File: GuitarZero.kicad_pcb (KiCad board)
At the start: 2 copper layers, 142 parts, among them J1 USB_A, J2 USB_B_Micro, J3 AudioJack3_SwitchT, J4 FPGA_Debug, J6 Micro_SD_Card_Det_Hirose_DM3AT, SW1 SW_Push, SW2 SW_Push, SW3 SW_Push, SW4 SW_Push, SW5 SW_Push, SW6 SW_Push, U1 TPS54325, U10 FPGA_GPIO_Extra, U11 5x7 LED_matrix, U12 MCU_GPIO_Extra, U13 5x7 LED_matrix, U14 Power_Jumpers, U2 TSP54294, U3 XC7A100T-FTG256, U4 EFM32GG332, U5 S25FL127S, U6 Oscillator, U7 FPGA_JTAG_Debug, U8 PCM1754, U9 TPD_Current_Switch, Y1 Crystal_GND23

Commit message: First pass at placing components physically
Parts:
- J4: value FPGA_Debug -> MCU_Debug
- moved U10 140.1 mm to (239.0, 67.2)
- moved R14 131.9 mm to (232.0, 97.0), turned to 180 degrees
- moved R15 131.9 mm to (232.0, 100.3), turned to 180 degrees
- moved R16 131.9 mm to (232.0, 103.6), turned to 180 degrees
- moved R17 131.8 mm to (232.0, 107.0)
- moved R13 131.8 mm to (232.0, 94.0), turned to 180 degrees
- moved U7 131.3 mm to (239.2, 93.2)
- moved U6 127.5 mm to (218.0, 80.0)
- moved R34 123.6 mm to (201.0, 72.4)
- moved R35 123.6 mm to (201.0, 75.7)
- moved U12 121.6 mm to (153.9, 180.0), turned to 90 degrees
- moved C53 120.7 mm to (222.0, 74.0)
- moved D1 116.9 mm to (209.9, 71.0)
- moved D2 116.9 mm to (209.9, 76.0)
- moved R29 104.8 mm to (136.0, 163.0), turned to 90 degrees
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
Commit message: Compression of intial placement
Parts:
- moved J4 77.3 mm to (156.5, 83.2)
- moved C35 74.8 mm to (256.6, 136.2)
- moved C36 74.8 mm to (256.6, 139.5)
- moved C40 74.8 mm to (265.6, 133.2)
- moved C41 74.8 mm to (265.6, 136.5)
- moved C49 74.8 mm to (274.6, 137.2)
- moved C50 74.8 mm to (274.6, 140.5)
- moved C37 74.8 mm to (256.6, 142.9)
- moved C38 74.8 mm to (265.6, 126.5)
- moved C39 74.8 mm to (265.6, 129.8)
- moved C42 74.8 mm to (265.6, 139.9)
- moved C43 74.8 mm to (265.6, 143.2)
- moved C44 74.8 mm to (274.6, 118.5)
- moved C45 74.8 mm to (274.6, 122.5)
- moved C46 74.8 mm to (274.6, 126.5)
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
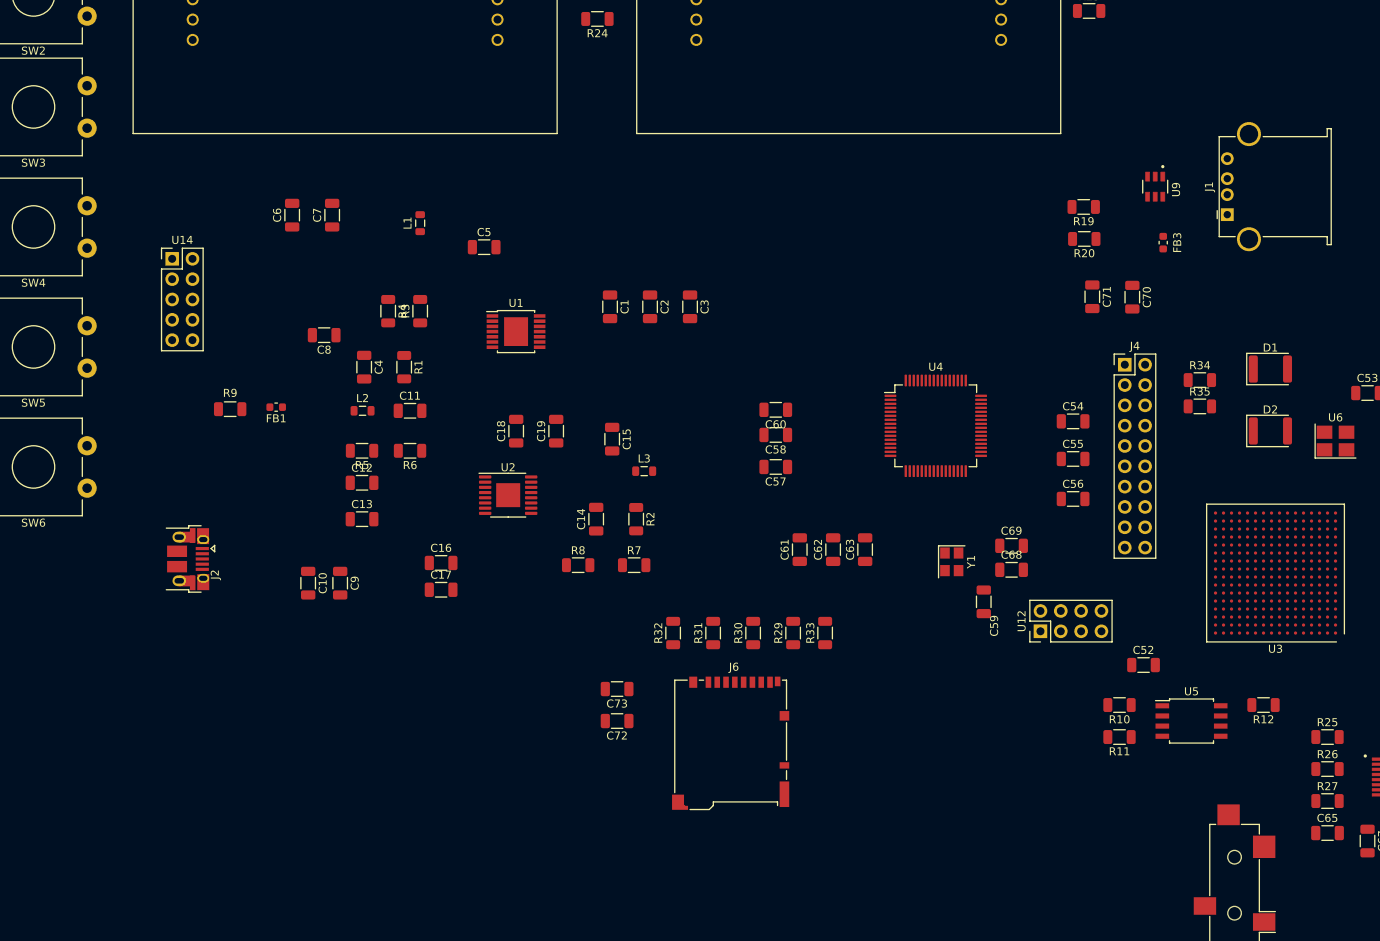
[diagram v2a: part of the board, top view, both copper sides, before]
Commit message: Improved space use for PCB
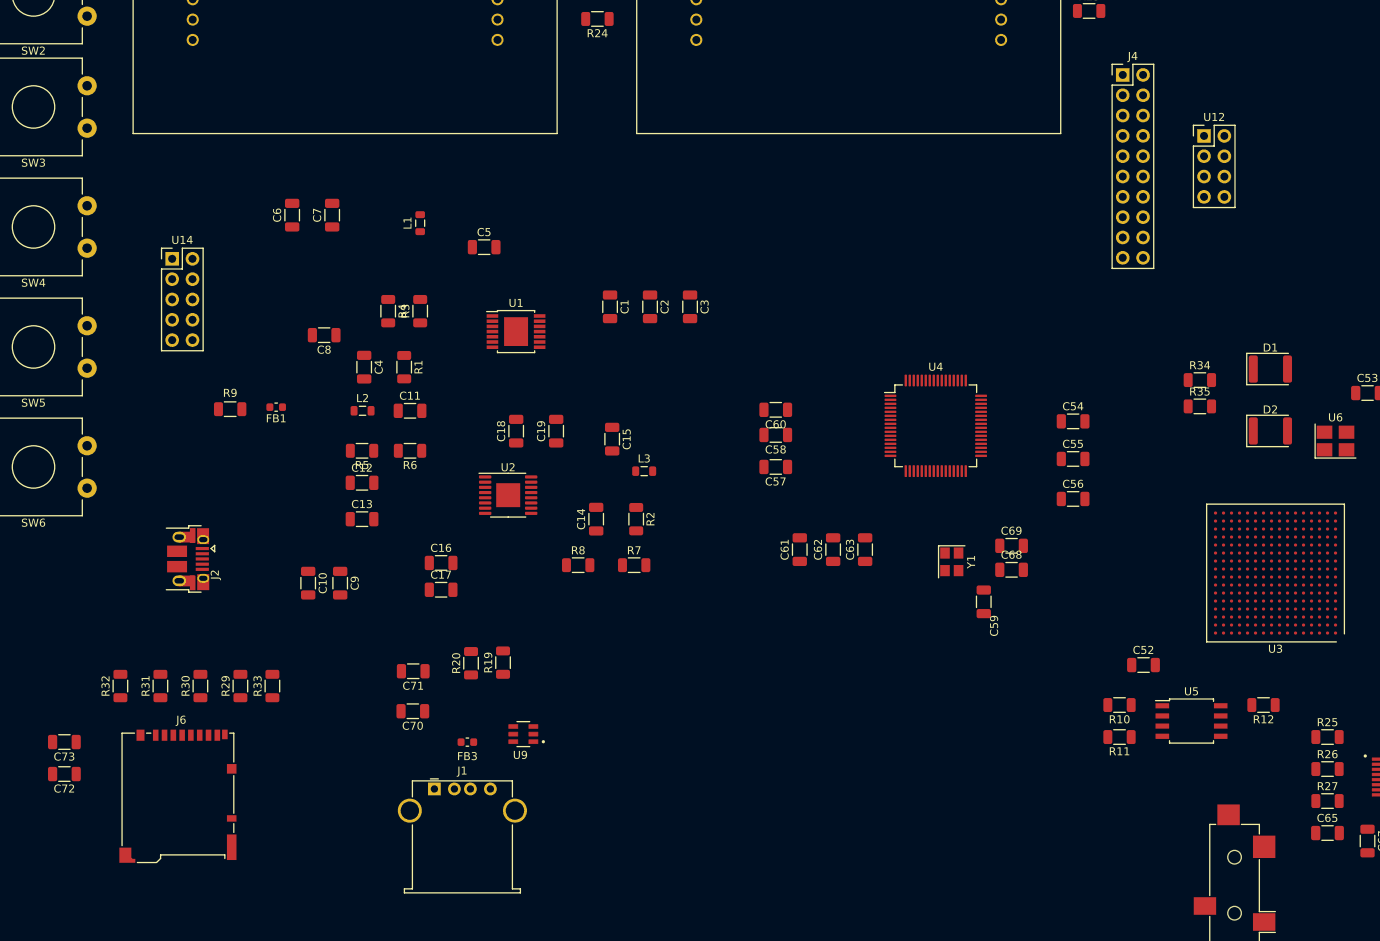
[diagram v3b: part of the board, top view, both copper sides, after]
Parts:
- moved J1 122.4 mm to (70.2, 136.2), turned to 0 degrees
- moved FB3 107.1 mm to (74.3, 130.4), turned to 180 degrees
- moved U9 104.5 mm to (81.3, 129.4), turned to 180 degrees
- moved C70 103.8 mm to (67.5, 126.5), turned to 180 degrees
- moved C71 96.9 mm to (67.5, 121.5), turned to 180 degrees
- moved R20 93.2 mm to (74.7, 120.5), turned to 90 degrees
- moved R19 92.3 mm to (78.7, 120.5), turned to 90 degrees
- moved C72 69.4 mm to (23.9, 134.4)
- moved C73 69.4 mm to (23.9, 130.4)
- moved J6 69.4 mm to (38.1, 137.2)
- moved R29 69.4 mm to (45.9, 123.4)
- moved R30 69.4 mm to (40.9, 123.4)
- moved R31 69.4 mm to (35.9, 123.4)
- moved R32 69.4 mm to (30.9, 123.4)
- moved R33 69.4 mm to (49.9, 123.4)
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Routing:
- added copper zone on In2.Cu, net GND
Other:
- copper layers 2 -> 6

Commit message: Placed components ready for wiring
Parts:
- C1, C10, C18, C19, C2, C20, C21, C22, C23, C24, C25, C26, C27, C28, C29, C3, C30, C31, C32, C33, C34, C35, C36, C37, C38, C39, C4, C40, C41, C42, C43, C44, C45, C46, C47, C48, C49, C5, C50, C51, C54, C55, C56, C57, C58, C59, C60, C61, C62, C63, C68, C69, C71, C8, C9, R1, R12, R13, R14, R15, R16, R17, R18, R21, R22, R23, R24, R3, R4: moved to B.Cu
- moved C71 115.4 mm to (177.0, 85.0), turned to 0 degrees
- moved C51 94.5 mm to (184.7, 115.0), turned to 180 degrees
- moved C44 94.5 mm to (184.7, 89.7), turned to 180 degrees
- moved C47 94.5 mm to (184.7, 101.7), turned to 180 degrees
- moved C48 94.5 mm to (184.7, 105.0), turned to 180 degrees
- moved C49 94.5 mm to (184.7, 108.3), turned to 180 degrees
- moved C50 94.5 mm to (184.7, 111.7), turned to 180 degrees
- moved C45 94.4 mm to (184.7, 93.7), turned to 180 degrees
- moved C46 94.4 mm to (184.7, 97.7), turned to 180 degrees
- moved C72 85.8 mm to (109.2, 125.0)
- moved C73 85.8 mm to (109.2, 121.0)
- moved C37 84.9 mm to (190.9, 89.1), turned to 90 degrees
- moved R32 83.6 mm to (114.2, 116.5)
- moved J6 83.0 mm to (121.0, 134.0)
- moved R31 82.4 mm to (118.1, 116.5)
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
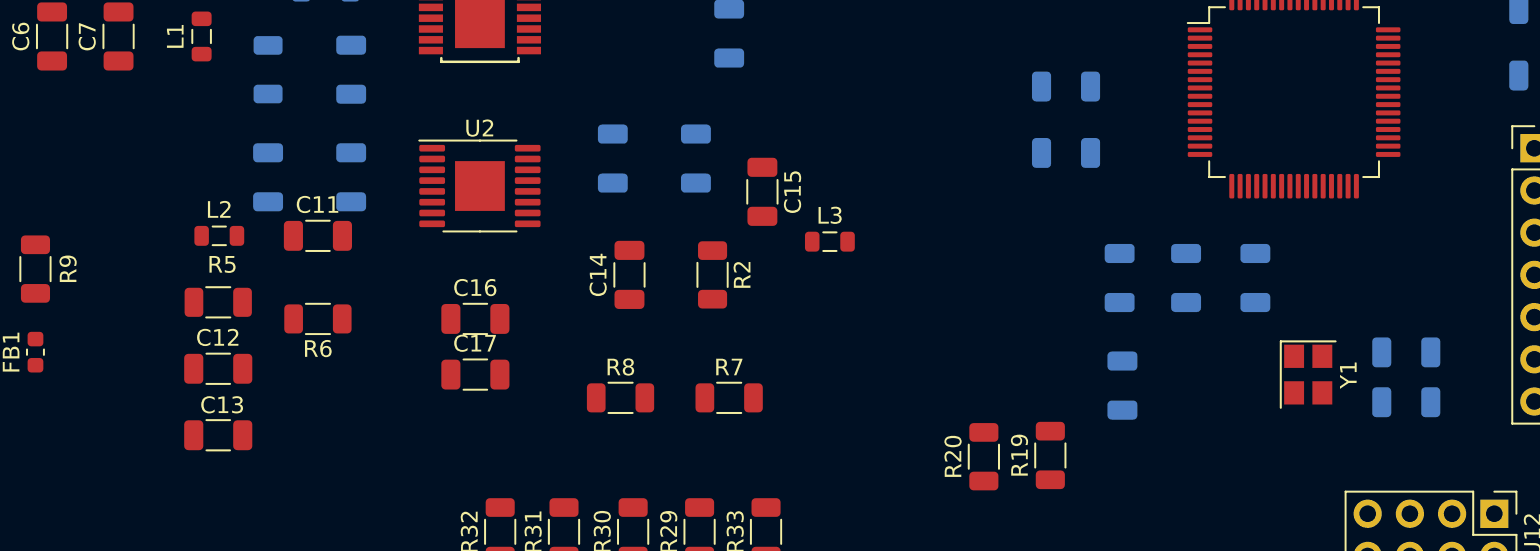
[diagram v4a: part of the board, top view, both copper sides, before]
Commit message: Moved some components for better power wiring
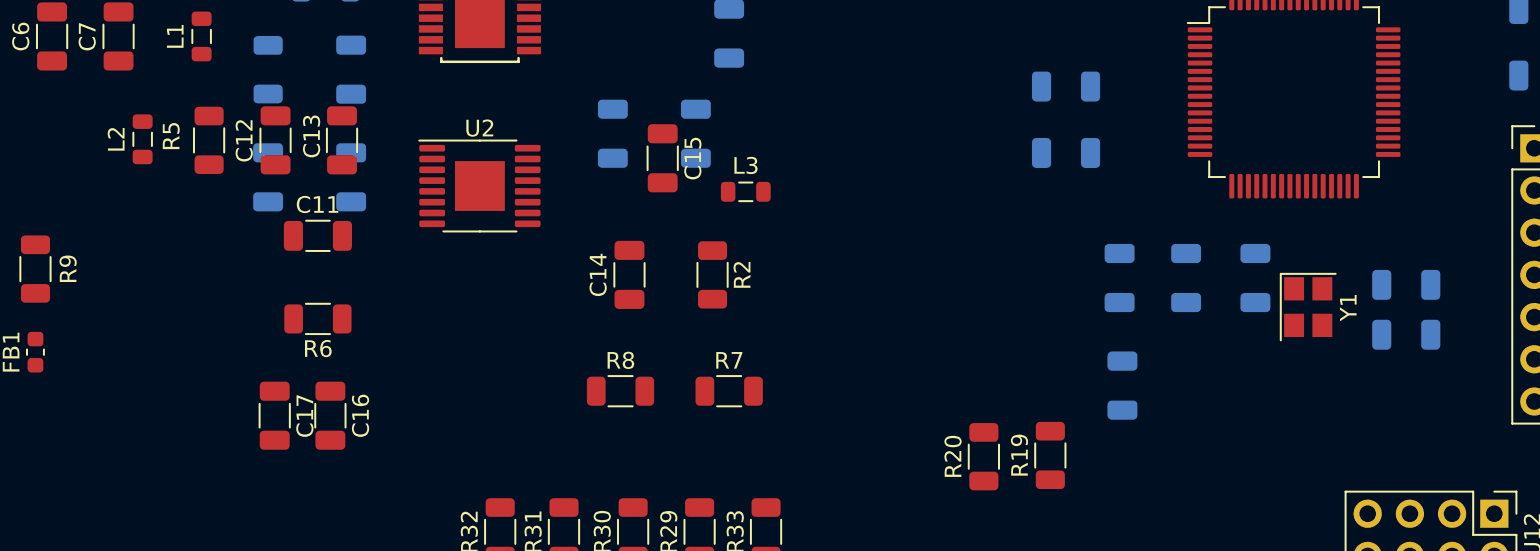
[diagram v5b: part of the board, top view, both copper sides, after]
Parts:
- moved C13 19.2 mm to (104.7, 92.9), turned to 90 degrees
- moved C12 14.2 mm to (100.7, 92.9), turned to 90 degrees
- moved C17 12.3 mm to (100.7, 109.5), turned to -90 degrees
- moved C16 10.5 mm to (104.0, 109.5), turned to -90 degrees
- moved R5 9.76 mm to (96.7, 92.9), turned to -90 degrees
- moved L2 7.42 mm to (92.7, 92.8), turned to 90 degrees
- moved C15 6.33 mm to (124.0, 94.0)
- moved L3 5.88 mm to (129.0, 96.0)
- moved C68 4.06 mm to (168.8, 104.6)
- moved C69 4.06 mm to (168.8, 101.6)
- moved Y1 4.06 mm to (162.8, 102.9)
- moved C18 1.50 mm to (121.0, 92.5)
- moved C19 1.50 mm to (126.0, 92.5)
- moved R7 0.40 mm to (128.0, 108.0)
- moved R8 0.40 mm to (121.5, 108.0)

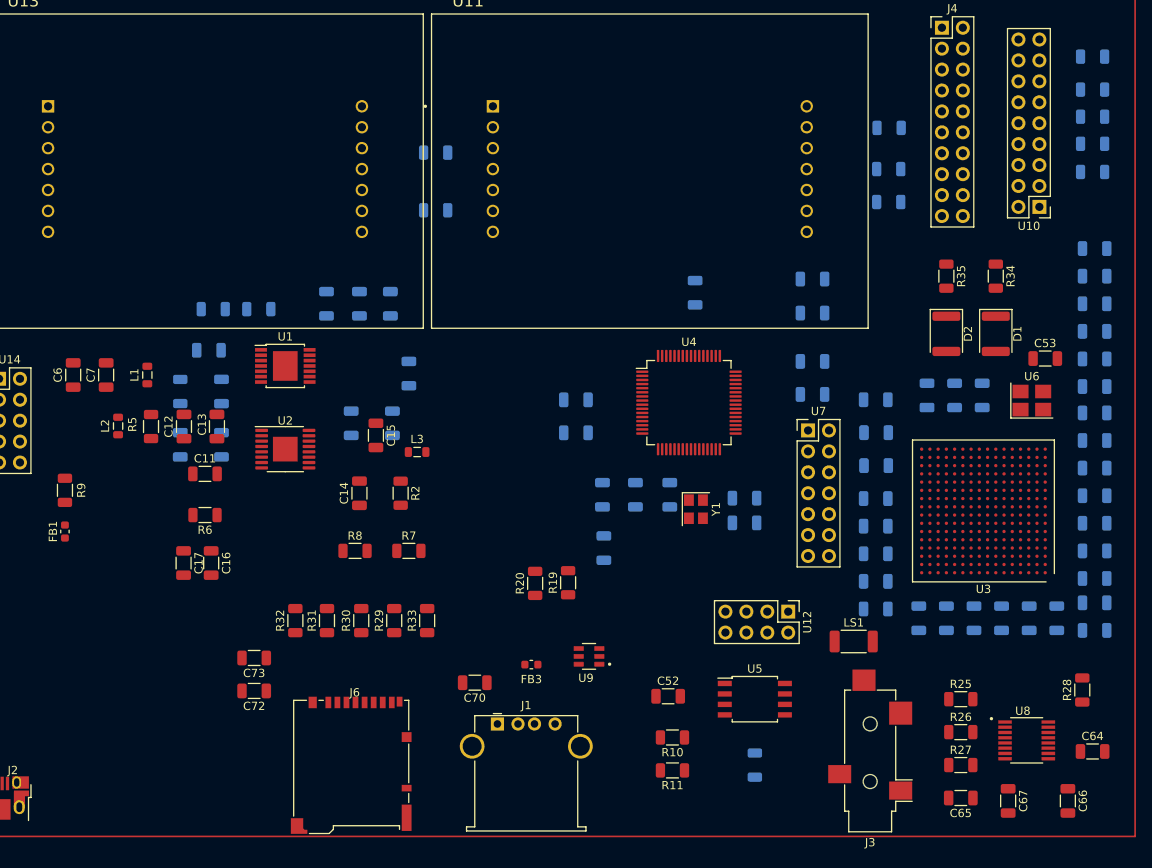
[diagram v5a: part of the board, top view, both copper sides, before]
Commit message: Changed Reistor and Capacitor size fomr 1206 to 0805
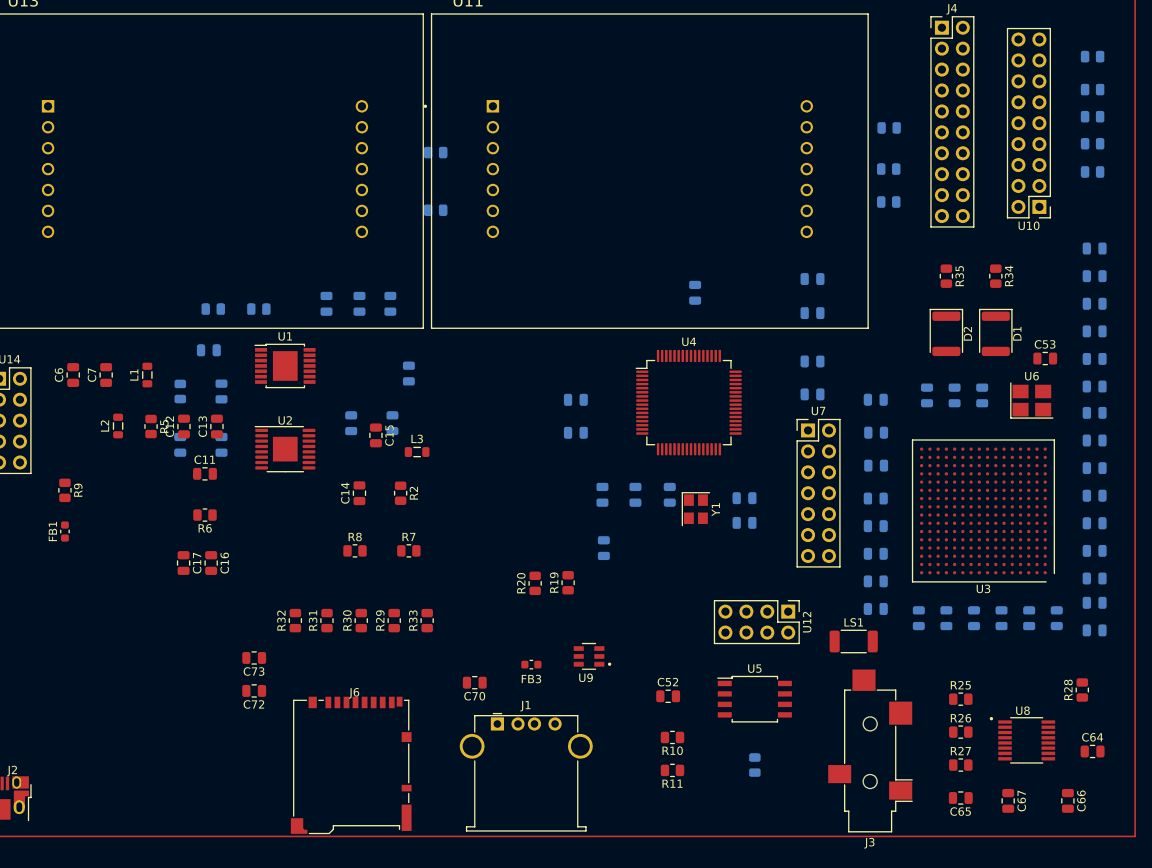
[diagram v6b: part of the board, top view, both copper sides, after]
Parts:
- C1, C10, C11, C12, C13, C14, C15, C16, C17, C18, C19, C2, C20, C21, C22, C23, C24, C25, C26, C27, C28, C29, C3, C30, C31, C32, C33, C34, C35, C36, C37, C38, C39, C4, C40, C41, C42, C43, C44, C45, C46, C47, C48, C49, C5, C50, C51, C52, C53, C54, C55, C56, C57, C58, C59, C6, C60, C61, C62, C63, C64, C65, C66, C67, C68, C69, C7, C70, C71, C72, C73, C8, C9: footprint Capacitor_SMD:C_1206_3216Metric -> Capacitor_SMD:C_0805_2012Metric
- R1, R10, R11, R12, R13, R14, R15, R16, R17, R18, R19, R2, R20, R21, R22, R23, R24, R25, R26, R27, R28, R29, R3, R30, R31, R32, R33, R34, R35, R4, R5, R6, R7, R8, R9: footprint Resistor_SMD:R_1206_3216Metric -> Resistor_SMD:R_0805_2012Metric

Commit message: Disconnected unused detect pins for SD card reader
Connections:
- J6 pad 10: GND -> unconnected-(J6-DET_A-Pad10)
- J6 pad 9: GND -> unconnected-(J6-DET_B-Pad9)
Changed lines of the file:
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@@
   (net 292 "Net-(J6-DAT0)")
   (net 293 "Net-(J6-DAT1)")
+  (net 294 "unconnected-(J6-DET_B-Pad9)")
+  (net 295 "unconnected-(J6-DET_A-Pad10)")
   (footprint "Inductor_SMD:L_0603_1608Metric" (layer "F.Cu")
     (at 142.87 121.805 180)
@@
       (net 293 "Net-(J6-DAT1)") (pinfunction "DAT1") (pintype "bidirectional"))
     (pad "9" smd rect (at 5.875 -7.725) (size 0.7 1.2) (layers "F.Cu" "F.Paste" "F.Mask")
-      (net 2 "GND") (pinfunction "DET_B") (pintype "passive"))
+      (net 294 "unconnected-(J6-DET_B-Pad9)") (pinfunction "DET_B") (pintype "passive+no_connect"))
     (pad "10" smd rect (at 6.725 2.775) (size 1.2 0.8) (layers "F.Cu" "F.Paste" "F.Mask")
-      (net 2 "GND") (pinfunction "DET_A") (pintype "passive"))
+      (net 295 "unconnected-(J6-DET_A-Pad10)") (pinfunction "DET_A") (pintype "passive+no_connect"))
     (pad "11" smd rect (at -6.575 7.375) (size 1.5 1.9) (layers "F.Cu" "F.Paste" "F.Mask")
       (net 2 "GND") (pinfunction "SHIELD") (pintype "passive"))
